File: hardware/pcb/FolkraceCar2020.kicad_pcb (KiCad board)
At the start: 2 copper layers, 65.8 x 56 mm, 26 parts, among them IC1 DRV8874PWPR, J3 Conn_01x03_Male, J4 Conn_01x02_Male, J5 Raspberry_Pi, Q1 BSS138, Q2 DMN10H220L, SW1 SPST, U1 TPS25940x-Q1, U2 OKL-T_6-W12N-C, U3 ADS1115IDGS

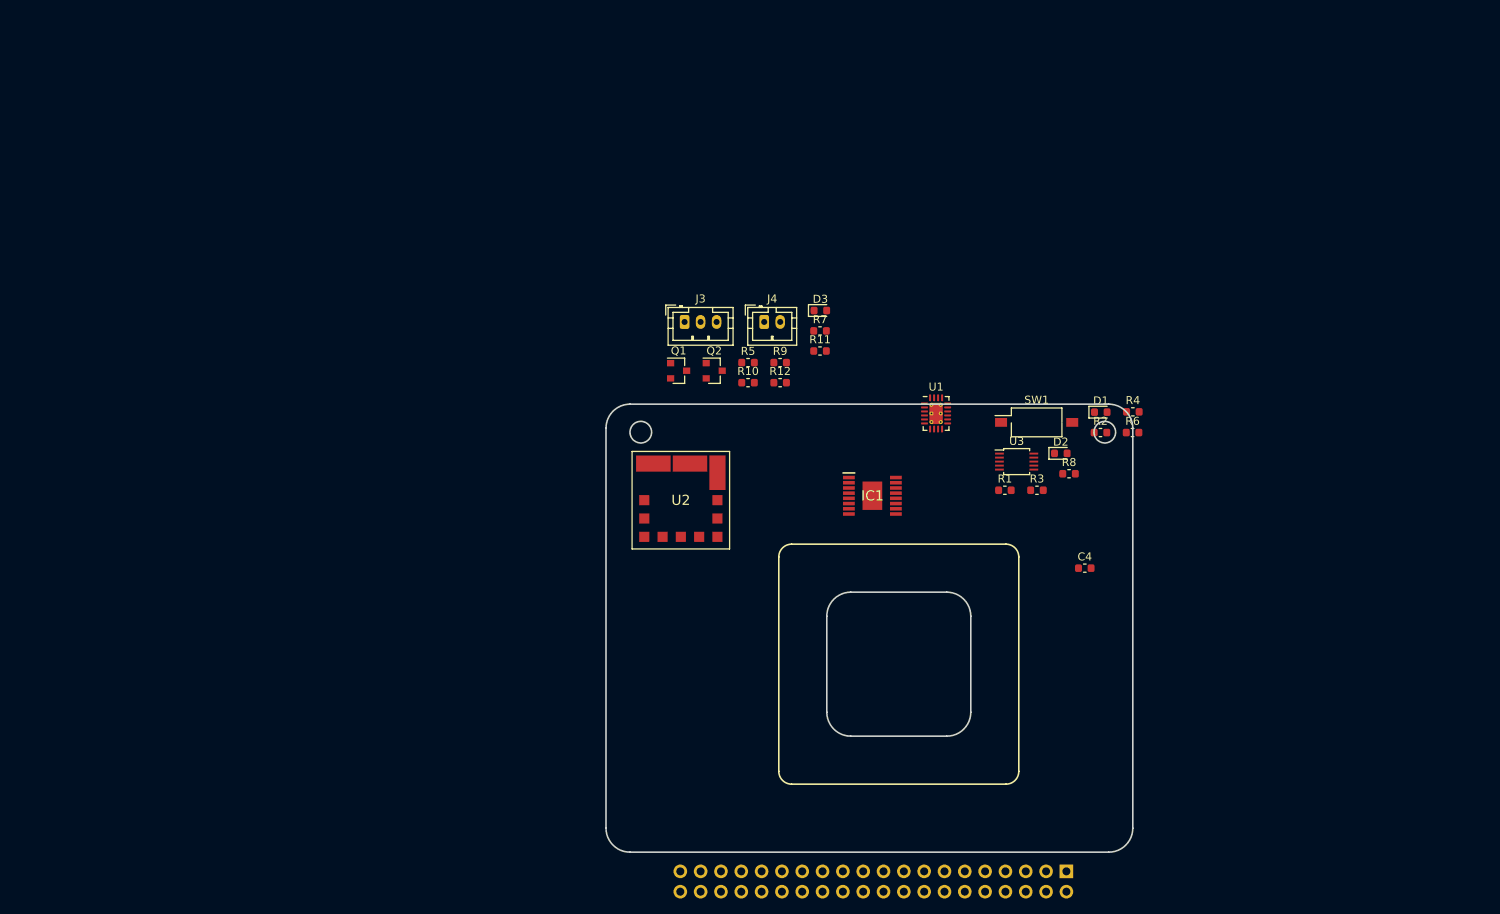
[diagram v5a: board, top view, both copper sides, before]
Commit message: started layout of PCB
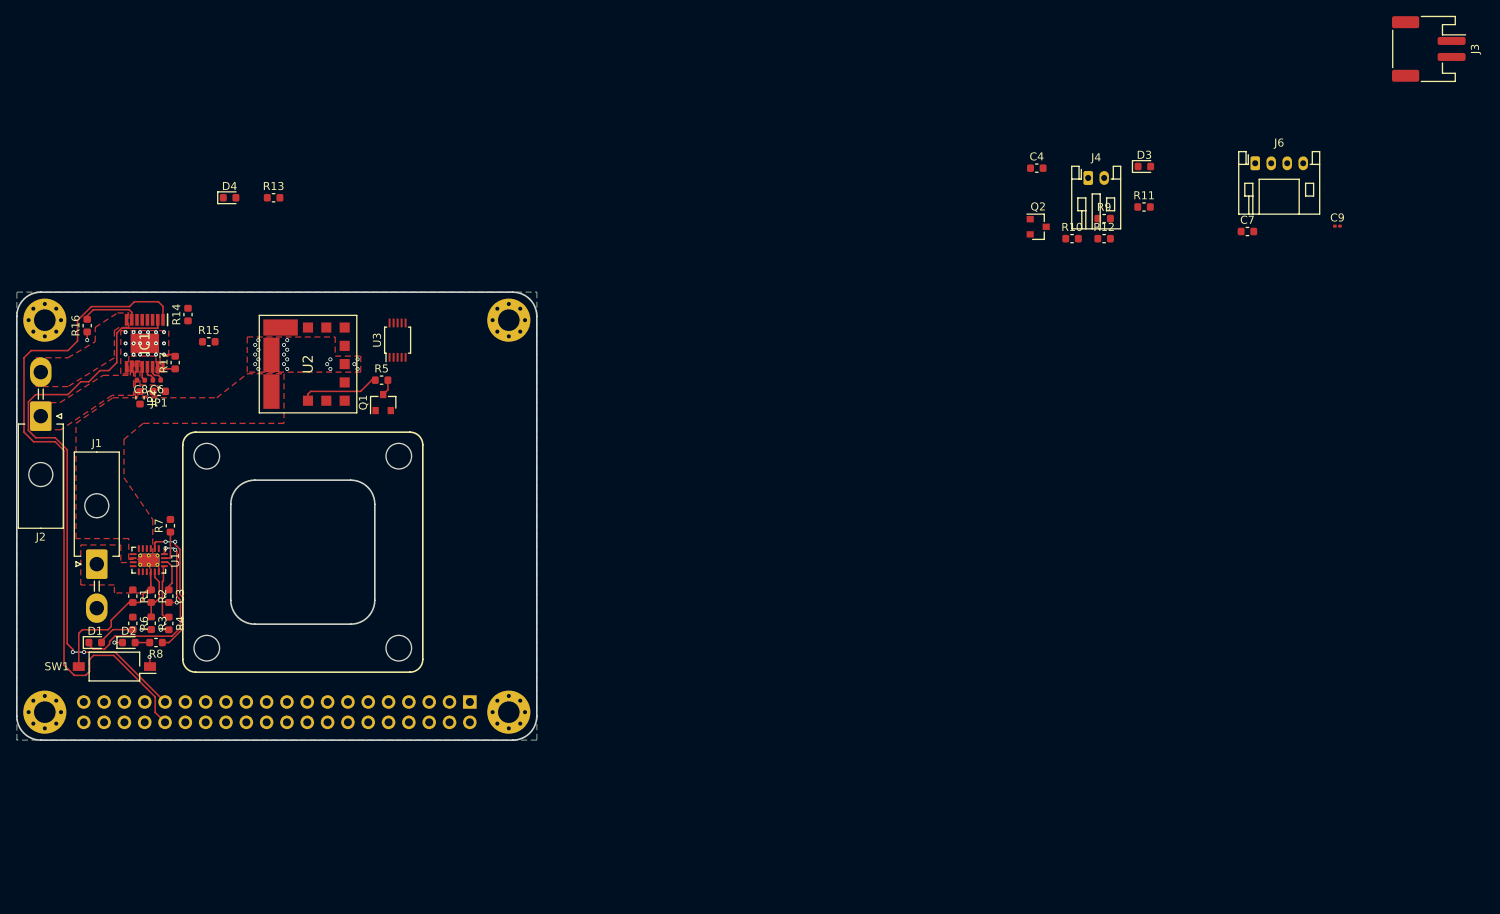
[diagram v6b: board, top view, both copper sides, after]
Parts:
- added C3: C, Capacitor_SMD:C_0603_1608Metric, F.Cu at (46.0, 110.0)
- added C6: 22nF X7R > 16 V, Capacitor_SMD:C_0402_1005Metric, F.Cu at (44.5, 83.0)
- added C7: C, Capacitor_SMD:C_0603_1608Metric, F.Cu at (180.8, 64.4)
- added C8: 100nF X7R > 16 V, Capacitor_SMD:C_0402_1005Metric, F.Cu at (42.5, 83.0)
- added C9: 100nF X7R > 16 V, Capacitor_SMD:C_0201_0603Metric, F.Cu at (192.1, 63.8)
- added D4: LED RED, LED_SMD:LED_0603_1608Metric, F.Cu at (53.6, 60.2)
- added H1: MountingHole_Pad, MountingHole:MountingHole_2.7mm_M2.5_Pad_Via, F.Cu at (30.5, 75.5)
- added H2: MountingHole_Pad, MountingHole:MountingHole_2.7mm_M2.5_Pad_Via, F.Cu at (88.5, 124.5)
- added H3: MountingHole_Pad, MountingHole:MountingHole_2.7mm_M2.5_Pad_Via, F.Cu at (88.5, 75.5)
- added H4: MountingHole_Pad, MountingHole:MountingHole_2.7mm_M2.5_Pad_Via, F.Cu at (30.5, 124.5)
- added H5: MountingHole, MountingHole:MountingHole_3.2mm_M3_ISO7380, F.Cu at (50.8, 92.5)
- added H6: MountingHole, MountingHole:MountingHole_3.2mm_M3_ISO7380, F.Cu at (50.8, 116.5)
- added H7: MountingHole, MountingHole:MountingHole_3.2mm_M3_ISO7380, F.Cu at (74.8, 92.5)
- added H8: MountingHole, MountingHole:MountingHole_3.2mm_M3_ISO7380, F.Cu at (74.8, 116.5)
- added J1: Conn_01x02_Male, Connector_Molex:Molex_Mini-Fit_Jr_5569-02A2_2x01_P4.20mm_Horizontal, F.Cu at (37.0, 106.0)
- added J2: Conn_01x02_Male, Connector_Molex:Molex_Mini-Fit_Jr_5569-02A2_2x01_P4.20mm_Horizontal, F.Cu at (30.0, 87.5)
- added J6: Conn Hall Effect, Connector_JST:JST_PH_S4B-PH-K_1x04_P2.00mm_Horizontal, F.Cu at (181.8, 55.9)
- added JP1: Jumper, Resistor_SMD:R_0603_1608Metric, F.Cu at (44.8, 84.4)
- added JP2: Jumper, Resistor_SMD:R_0603_1608Metric, F.Cu at (42.4, 85.2)
- added R13: R, Resistor_SMD:R_0603_1608Metric, F.Cu at (59.1, 60.2)
- added R14: R, Resistor_SMD:R_0603_1608Metric, F.Cu at (48.4, 74.8)
- added R15: R, Resistor_SMD:R_0603_1608Metric, F.Cu at (51.0, 78.2)
- added R16: R, Resistor_SMD:R_0603_1608Metric, F.Cu at (35.8, 76.2)
- added R17: R, Resistor_SMD:R_0603_1608Metric, F.Cu at (46.8, 80.8)
- J3: value Conn_01x03_Male -> Conn Servo; footprint Connector_JST:JST_PH_B3B-PH-K_1x03_P2.00mm_Vertical -> Connector_JST:JST_PH_S2B-PH-SM4-TB_1x02-1MP_P2.00mm_Horizontal
- J4: value Conn_01x02_Male -> Conn Fan; footprint Connector_JST:JST_PH_B2B-PH-K_1x02_P2.00mm_Vertical -> Connector_JST:JST_PH_S2B-PH-K_1x02_P2.00mm_Horizontal
- moved D1 129.0 mm to (36.8, 115.8)
- moved R6 127.2 mm to (41.5, 113.4), turned to 270 degrees
- moved R4 123.4 mm to (46.0, 113.4), turned to 270 degrees
- moved R2 120.4 mm to (43.8, 110.0), turned to 270 degrees
- moved SW1 119.3 mm to (39.2, 118.8), turned to 180 degrees
- moved D2 118.9 mm to (41.0, 115.8)
- moved R8 116.1 mm to (44.4, 115.8), turned to 180 degrees
- moved R3 112.0 mm to (43.8, 113.4), turned to 270 degrees
- moved R1 109.8 mm to (41.5, 110.0), turned to 270 degrees
- moved U1 100.1 mm to (43.5, 105.5), turned to 270 degrees
- moved J3 99.1 mm to (203.5, 41.6), turned to 270 degrees
- moved IC1 92.9 mm to (43.0, 78.4), turned to 270 degrees
- moved R7 84.8 mm to (46.2, 101.2), turned to 90 degrees
- moved U3 78.9 mm to (74.6, 78.0), turned to 90 degrees
- moved J5 77.5 mm to (83.6, 123.2)
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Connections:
- IC1 pad 1: Net-(IC1-Pad1) -> /PWM_M
- IC1 pad 10: Net-(IC1-Pad10) -> /M2
- IC1 pad 11: Net-(IC1-Pad11) -> /VM
- IC1 pad 15: Net-(IC1-Pad15) -> GND
- IC1 pad 17: Net-(IC1-Pad17) -> GND
- IC1 pad 2: Net-(IC1-Pad2) -> /DIR_M
- IC1 pad 5: Net-(IC1-Pad5) -> +3V3
- IC1 pad 6: Net-(IC1-Pad6) -> /IMON_M
- IC1 pad 8: Net-(IC1-Pad8) -> /M1
- IC1 pad 9: Net-(IC1-Pad9) -> GND
- J3 pad 2: /SERVO_PWM -> (no net)
- J5 pad 10: Net-(J5-Pad10) -> (no net)
- J5 pad 11: Net-(J5-Pad11) -> (no net)
- J5 pad 12: Net-(J5-Pad12) -> (no net)
- J5 pad 13: Net-(J5-Pad13) -> (no net)
- J5 pad 15: Net-(J5-Pad15) -> (no net)
- J5 pad 16: Net-(J5-Pad16) -> (no net)
- J5 pad 18: Net-(J5-Pad18) -> (no net)
- J5 pad 19: Net-(J5-Pad19) -> (no net)
- J5 pad 21: Net-(J5-Pad21) -> (no net)
- J5 pad 22: Net-(J5-Pad22) -> (no net)
- J5 pad 23: Net-(J5-Pad23) -> (no net)
- J5 pad 24: Net-(J5-Pad24) -> (no net)
- J5 pad 26: Net-(J5-Pad26) -> (no net)
- J5 pad 27: Net-(J5-Pad27) -> (no net)
- J5 pad 28: Net-(J5-Pad28) -> (no net)
- J5 pad 29: Net-(J5-Pad29) -> (no net)
- J5 pad 3: Net-(J5-Pad3) -> /SDA
- J5 pad 31: Net-(J5-Pad31) -> /DIR_M
- J5 pad 32: Net-(J5-Pad32) -> /PWM_M
- J5 pad 33: Net-(J5-Pad33) -> (no net)
- J5 pad 35: Net-(J5-Pad35) -> (no net)
- J5 pad 36: Net-(J5-Pad36) -> (no net)
- J5 pad 37: Net-(J5-Pad37) -> (no net)
- J5 pad 38: Net-(J5-Pad38) -> (no net)
- J5 pad 40: Net-(J5-Pad40) -> (no net)
- J5 pad 5: Net-(J5-Pad5) -> /SCL
- J5 pad 7: Net-(J5-Pad7) -> (no net)
- J5 pad 8: Net-(J5-Pad8) -> (no net)
- Q2 pad 1: /FAN_CTRL -> (no net)
- U1 pad 1: Net-(U1-Pad1) -> (no net)
- U2 pad 11: Net-(U2-Pad11) -> (no net)
- U2 pad 12: Net-(U2-Pad12) -> (no net)
- U2 pad 8: Net-(U2-Pad8) -> (no net)
- U2 pad 9: Net-(U2-Pad9) -> (no net)
- U3 pad 1: Net-(U3-Pad1) -> (no net)
- U3 pad 10: Net-(U3-Pad10) -> /SCL
- U3 pad 2: Net-(U3-Pad2) -> (no net)
- U3 pad 6: Net-(U3-Pad6) -> /IMON_M
- U3 pad 7: Net-(U3-Pad7) -> (no net)
- U3 pad 9: Net-(U3-Pad9) -> /SDA
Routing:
- net /PWM_M: track 0.00 -> 85.4 mm
- net /DIR_M: track 0.00 -> 72.3 mm, vias 0 -> 2
- net Net-(D1-Pad1): track 0.00 -> 25.5 mm, vias 0 -> 2
- net Net-(R1-Pad2): track 0.00 -> 18.6 mm
- net Net-(Q1-Pad1): track 0.00 -> 17.9 mm, vias 0 -> 2
- net Net-(R5-Pad1): track 0.00 -> 9.97 mm
- net GND: track 0.00 -> 8.91 mm, vias 0 -> 44
- net Net-(IC1-Pad7): track 0.00 -> 7.40 mm
- net Net-(R4-Pad1): track 0.00 -> 7.09 mm
- net Net-(R2-Pad2): track 0.00 -> 6.57 mm
- net Net-(D1-Pad2): track 0.00 -> 4.50 mm
- net Net-(C3-Pad1): track 0.00 -> 4.29 mm
- net /IMON: track 0.00 -> 3.98 mm
- net Net-(C6-Pad1): track 0.00 -> 2.36 mm
- net Net-(C6-Pad2): track 0.00 -> 2.12 mm
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- added copper zone on F.Cu, net +BATT
- added copper zone on F.Cu, net /M1
- added copper zone on F.Cu, net /M2
- added copper zone on F.Cu, net /VM
- added copper zone on B.Cu, net GND
- added copper zone on F.Cu, net GND
- added copper zone on F.Cu, net VBUS
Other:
- board size 65.8 x 56 mm -> 65 x 56 mm
- net class Default: clearance 0.2 -> 0.1; trace_width 0.25 -> 0.2; via_dia 0.8 -> 0.5; via_drill 0.4 -> 0.3
- rule trace_clearance: 0.2 -> 0.1
- rule trace_min: 0.2 -> 0.1
- rule via_min_size: 0.4 -> 0.45

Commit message: extended pcb outline
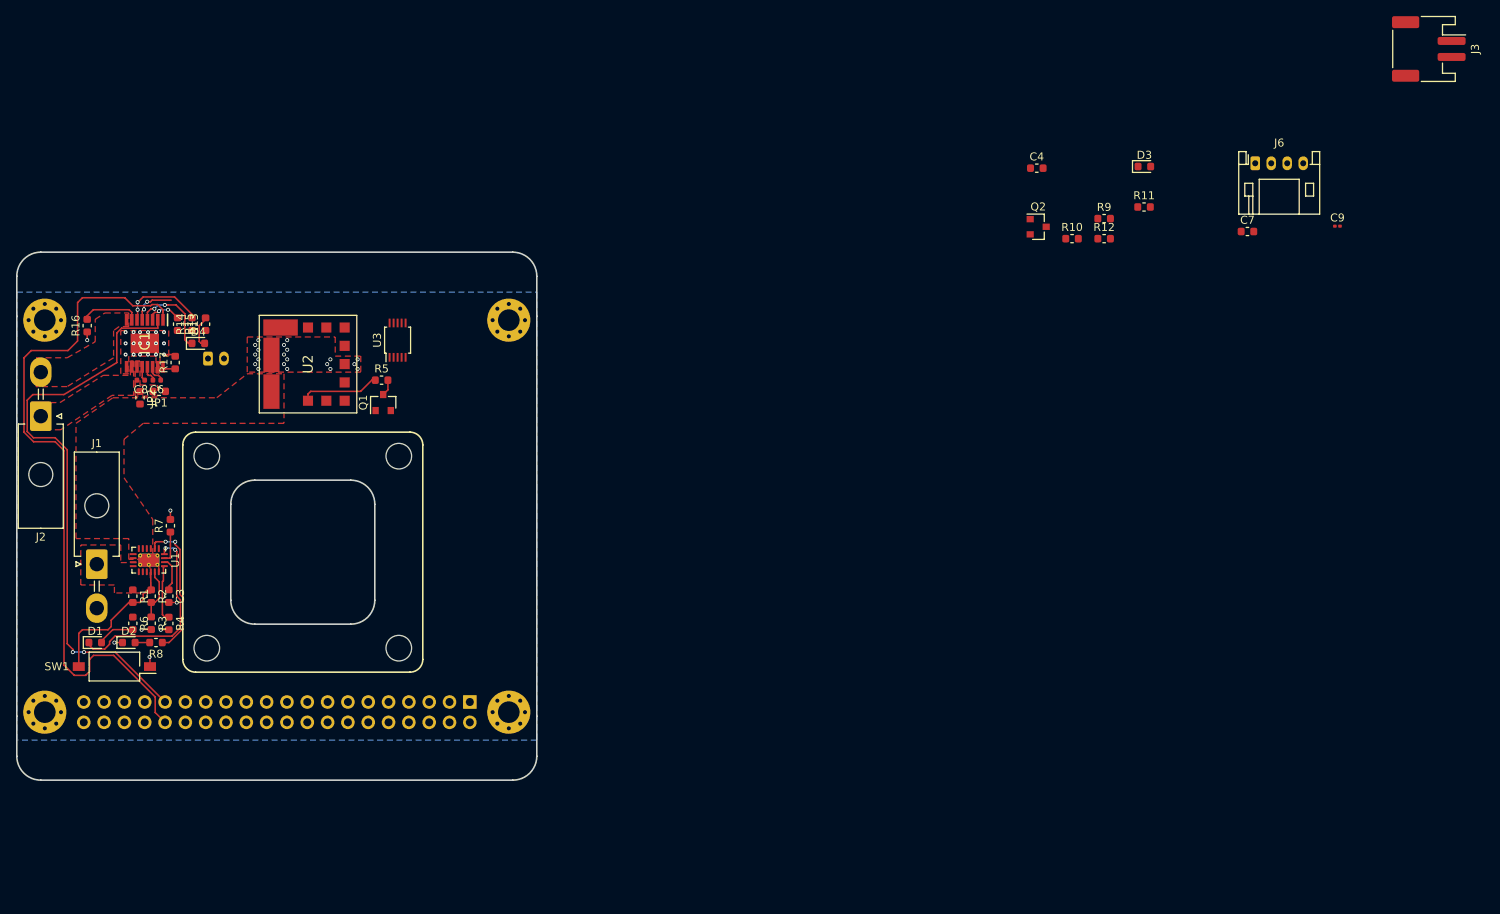
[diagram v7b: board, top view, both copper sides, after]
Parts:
- J4: moved to B.Cu
- moved J4 112.3 mm to (50.9, 80.3)
- moved D4 18.6 mm to (49.7, 78.4)
- moved R13 17.9 mm to (50.6, 76.0), turned to 90 degrees
- moved R15 4.48 mm to (47.1, 76.0), turned to 270 degrees
- moved R14 1.30 mm to (48.9, 76.0)
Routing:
- net Net-(D4-Pad1): track 0.00 -> 10.8 mm, vias 0 -> 2
- net /IMON_M: track 0.00 -> 10.7 mm, vias 0 -> 2
- net +3V3: track 0.00 -> 5.60 mm, vias 0 -> 2
- net Net-(IC1-Pad3): track 0.00 -> 4.46 mm, vias 0 -> 2
- net Net-(D4-Pad2): track 0.00 -> 4.05 mm
- net /PWM_M: track 85.4 -> 87.0 mm
- net GND: track 8.91 -> 10.0 mm, vias 44 -> 45
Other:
- board size 65 x 56 mm -> 65 x 66 mm

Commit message: worked on pcb layout. Some Schematic def. still to be done
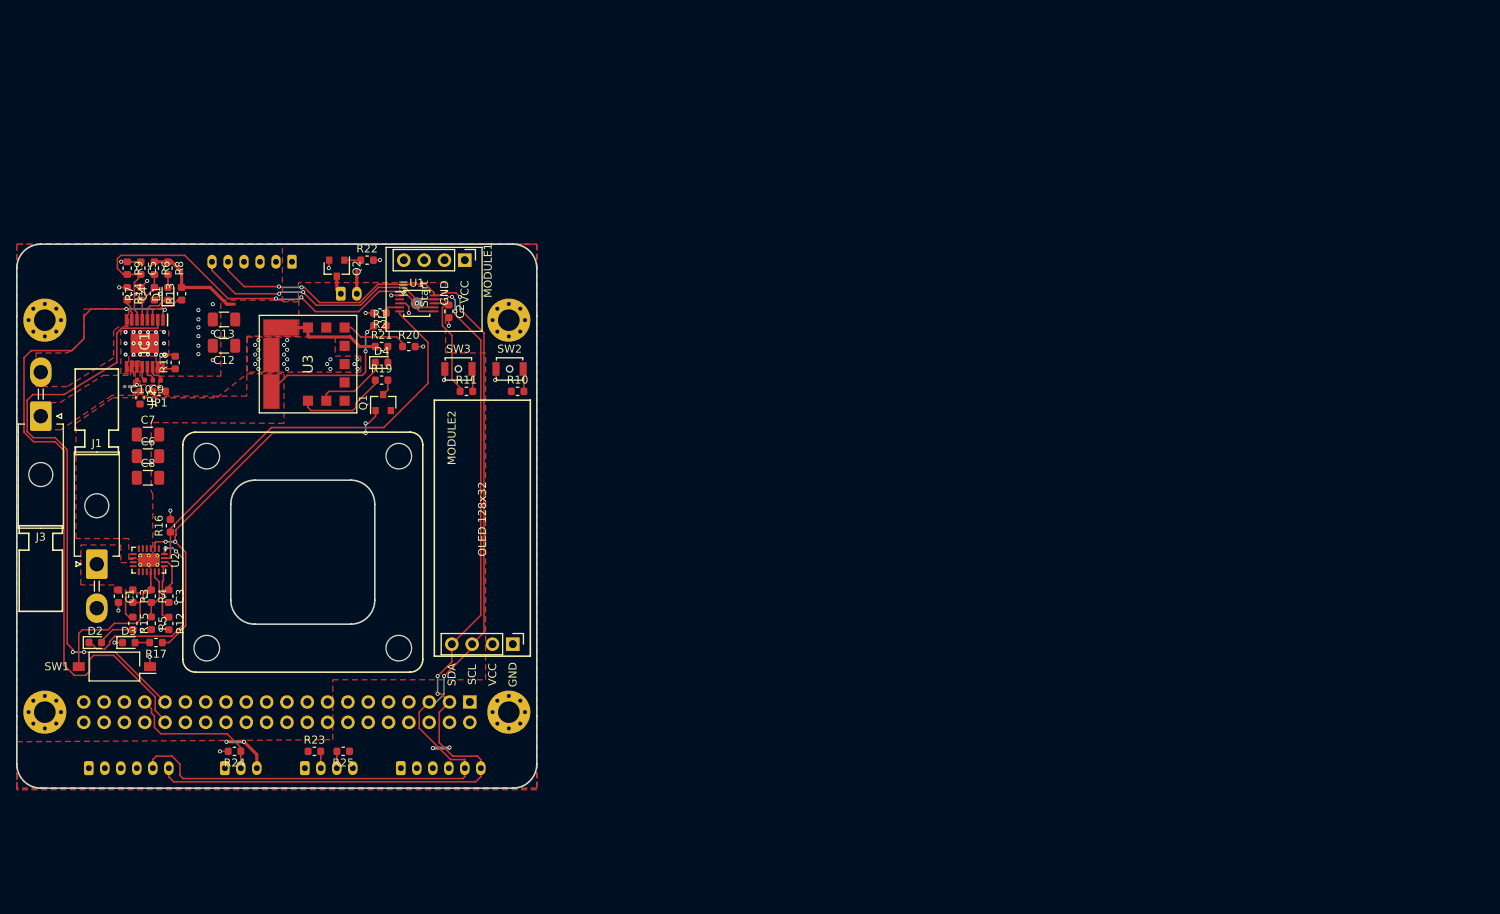
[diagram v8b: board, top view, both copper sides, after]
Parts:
- removed the R9 at (162.9, 62.8)
- removed the U3 at (74.6, 78.0)
- added C1: C, Capacitor_SMD:C_0603_1608Metric, F.Cu at (39.7, 110.0)
- added C12: C, Capacitor_SMD:C_1206_3216Metric, F.Cu at (52.9, 78.7)
- added C13: C, Capacitor_SMD:C_1206_3216Metric, F.Cu at (52.9, 75.4)
- added C4: C, Capacitor_SMD:C_0603_1608Metric, F.Cu at (44.2, 72.2)
- added C6: C, Capacitor_SMD:C_1206_3216Metric, F.Cu at (43.4, 92.5)
- added C7: C, Capacitor_SMD:C_1206_3216Metric, F.Cu at (43.4, 89.8)
- added C8: C, Capacitor_SMD:C_1206_3216Metric, F.Cu at (43.4, 95.2)
- added J7: Conn_01x06_Male, Connector_JST:JST_PH_B6B-PH-K_1x06_P2.00mm_Vertical, B.Cu at (75.0, 131.5)
- added J8: Conn_01x06_Male, Connector_JST:JST_PH_B6B-PH-K_1x06_P2.00mm_Vertical, B.Cu at (36.0, 131.5)
- added J9: Conn_01x06_Male, Connector_JST:JST_PH_B6B-PH-K_1x06_P2.00mm_Vertical, B.Cu at (61.4, 68.2)
- added MODULE1: Startmodule, Connector_PinHeader_2.54mm:PinHeader_1x04_P2.54mm_Vertical, F.Cu at (83.0, 68.0)
- added MODULE2: OLED 128x32, Connector_PinHeader_2.54mm:PinHeader_1x04_P2.54mm_Vertical, F.Cu at (89.0, 116.0)
- added R10: R, Resistor_SMD:R_0603_1608Metric, F.Cu at (89.6, 84.4)
- added R11: R, Resistor_SMD:R_0603_1608Metric, F.Cu at (83.2, 84.4)
- added R20: 1.3k, Resistor_SMD:R_0603_1608Metric, F.Cu at (76.0, 78.8)
- added R22: R, Resistor_SMD:R_0603_1608Metric, F.Cu at (70.8, 68.0)
- added R23: R, Resistor_SMD:R_0603_1608Metric, F.Cu at (64.2, 129.4)
- added R24: R, Resistor_SMD:R_0603_1608Metric, F.Cu at (54.2, 129.4)
- added R25: R, Resistor_SMD:R_0603_1608Metric, F.Cu at (67.8, 129.4)
- added R6: R, Resistor_SMD:R_0603_1608Metric, F.Cu at (44.2, 69.0)
- added R7: R, Resistor_SMD:R_0603_1608Metric, F.Cu at (42.5, 72.2)
- added SW2: SW_Push, Button_Switch_SMD:SW_SPST_B3U-1000P-B, F.Cu at (88.6, 81.6)
- added SW3: SW_Push, Button_Switch_SMD:SW_SPST_B3U-1000P-B, F.Cu at (82.2, 81.6)
- added TP1: TestPoint, TestPoint:TestPoint_Pad_D1.5mm, B.Cu at (77.0, 73.4)
- added U1: ADS1115IDGS, Package_SO:TSSOP-10_3x3mm_P0.5mm, F.Cu at (77.0, 73.4)
- C11: renamed from C9; moved to B.Cu
- J4: renamed from J3; footprint Connector_JST:JST_PH_S2B-PH-SM4-TB_1x02-1MP_P2.00mm_Horizontal -> Connector_JST:JST_PH_B3B-PH-K_1x03_P2.00mm_Vertical; moved to B.Cu
- J6: footprint Connector_JST:JST_PH_S4B-PH-K_1x04_P2.00mm_Horizontal -> Connector_JST:JST_PH_B4B-PH-K_1x04_P2.00mm_Vertical; moved to B.Cu
- moved J4 175.3 mm to (53.0, 131.5), turned to 0 degrees
- moved C11 152.6 mm to (40.8, 83.8), turned to 180 degrees
- moved J6 140.8 mm to (63.0, 131.5)
- moved C5 138.4 mm to (42.5, 69.0), turned to 270 degrees
- moved D4 98.4 mm to (72.6, 80.8)
- moved R1 96.7 mm to (72.4, 76.2)
- moved R2 91.0 mm to (72.4, 74.6), turned to 180 degrees
- moved Q2 87.8 mm to (67.0, 69.0), turned to 270 degrees
- moved R21 87.4 mm to (72.6, 78.8)
- moved C2 75.6 mm to (81.0, 74.4), turned to 270 degrees
- moved J5 18.5 mm to (67.5, 72.2)
- moved R9 10.7 mm to (40.8, 69.0), turned to 270 degrees
- moved R8 8.43 mm to (45.9, 69.0), turned to 270 degrees
- moved D1 7.27 mm to (45.9, 72.2), turned to 90 degrees
- moved R14 6.40 mm to (40.8, 72.2), turned to 270 degrees
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- renumbered C8 to C10, C4 to C2, C7 to C5, C6 to C9, D4 to D1, D1 to D2, D2 to D3, D3 to D4, H5 to H1, H6 to H2, H1 to H3, H2 to H4, H7 to H5, H8 to H6, H3 to H7, H4 to H8, J5 to J2, J2 to J3, J4 to J5, R11 to R1, R4 to R12, R15 to R13, R16 to R14, R6 to R15, R7 to R16, R8 to R17, R17 to R18, R5 to R19, R12 to R2, R10 to R21, R1 to R3, R2 to R4, R3 to R5, R13 to R8, R14 to R9, U1 to U2, U2 to U3
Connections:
- net Net-(J4-Pad1) renamed /FAN-
- C2 pad 1: +3V3 -> +5V
- IC1 pad 5: +3V3 -> Net-(C4-Pad2)
- J2 pad 1: +3V3 -> (no net)
- J2 pad 17: +3V3 -> (no net)
- J2 pad 33: (no net) -> /SERVO_PWM
- J4 pad 2: (no net) -> /SERVO_PWM
- J6 pad 2: (no net) -> /ME_B
- J6 pad 3: (no net) -> /ME_A
- Q2 pad 1: (no net) -> /FAN_CTRL
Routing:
- net /SCL: track 0.00 -> 145.2 mm, vias 0 -> 5
- net /SDA: track 0.00 -> 144.9 mm, vias 0 -> 6
- net +5V: track 0.00 -> 52.2 mm, vias 0 -> 4
- net /IMON: track 3.98 -> 54.6 mm
- net /IMON_M: track 10.7 -> 55.8 mm
- net Net-(Q1-Pad1): track 17.9 -> 51.9 mm, vias 2 -> 4
- net VBUS: track 0.00 -> 19.1 mm, vias 0 -> 2
- net /SERVO_PWM: track 0.00 -> 18.1 mm
- net GND: track 10.0 -> 23.5 mm, vias 45 -> 67
- net Net-(D4-Pad1): track 0.00 -> 9.17 mm
- net Net-(R20-Pad1): track 0.00 -> 8.50 mm
- net Net-(C4-Pad2): track 0.00 -> 6.58 mm
- net Net-(D1-Pad1): track 10.8 -> 4.41 mm, vias 2 -> 0
- net +3V3: track 5.60 -> 0.00 mm, vias 2 -> 0
- net Net-(IC1-Pad7): track 7.40 -> 2.71 mm
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- added copper zone on F.Cu, net +5V
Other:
- board size 65 x 66 mm -> 65 x 68 mm
- net class Default: clearance 0.1 -> 0.127
- net class PWR added: clearance 0.127, trace_width 0.4, via_dia 0.5, via_drill 0.3
- rule trace_clearance: 0.1 -> 0.127
- rule trace_min: 0.1 -> 0.127
- rule via_min_drill: 0.3 -> 0.2
